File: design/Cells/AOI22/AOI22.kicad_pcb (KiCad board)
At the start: 2 copper layers, 8 parts, among them P1 Q_PJFET_GSD, P2 Q_PJFET_GSD, P3 Q_PJFET_GSD, P4 Q_PJFET_GSD

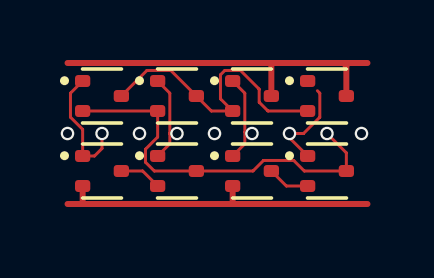
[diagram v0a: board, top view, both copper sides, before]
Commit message: Swap A and B pads in NAND footprint Polishing of AOI22 PCB, proper placement of the pins
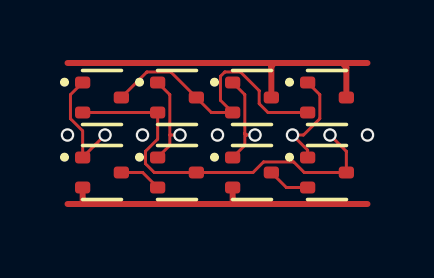
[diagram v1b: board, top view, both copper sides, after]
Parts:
- moved N1 0.05 mm to (1.15, 3.60)
- moved N2 0.05 mm to (3.65, 3.60)
- moved N3 0.05 mm to (6.15, 3.60)
- moved N4 0.05 mm to (8.65, 3.60)
- moved P1 0.05 mm to (1.15, 1.10)
- moved P2 0.05 mm to (3.65, 1.10)
- moved P3 0.05 mm to (6.15, 1.10)
- moved P4 0.05 mm to (8.65, 1.10)

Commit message: All gates layout on a strict 2.5mm grid. Flipped versions of all three layouts
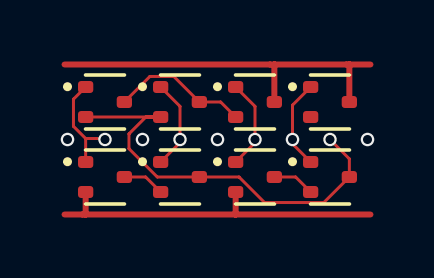
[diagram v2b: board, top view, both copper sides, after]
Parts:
- moved N1 0.18 mm to (1.25, 3.75)
- moved N2 0.18 mm to (3.75, 3.75)
- moved P1 0.18 mm to (1.25, 1.25)
- moved P2 0.18 mm to (3.75, 1.25)
- moved N3 0.18 mm to (6.25, 3.75)
- moved N4 0.18 mm to (8.75, 3.75)
- moved P3 0.18 mm to (6.25, 1.25)
- moved P4 0.18 mm to (8.75, 1.25)
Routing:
- net Net-(P1-D): track 9.78 -> 4.62 mm
- net Y: track 13.0 -> 14.2 mm
- net GND: track 11.1 -> 11.7 mm
- net D: track 3.54 -> 3.00 mm

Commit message: flip the cells to share power lines
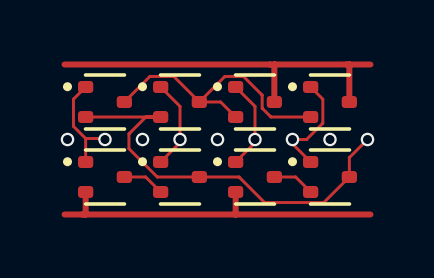
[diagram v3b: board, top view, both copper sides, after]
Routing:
- net Net-(P1-D): track 4.62 -> 9.50 mm
- net D: track 3.00 -> 3.61 mm
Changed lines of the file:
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@@
 	)
 	(via
-		(at 10 2.5)
+		(at 5 2.5)
 		(size 0.45)
 		(drill 0.3)
@@
 	)
 	(via
-		(at 5 2.5)
+		(at 0 2.5)
 		(size 0.45)
 		(drill 0.3)
@@
 	)
 	(via
-		(at 0 2.5)
+		(at 8.75 2.5)
 		(size 0.45)
 		(drill 0.3)
@@
 	)
 	(segment
+		(start 9.395 3.75)
+		(end 9.395 3.105)
+		(width 0.1)
+		(layer "F.Cu")
+		(net 5)
+	)
+	(segment
 		(start 6.568738 4.601)
 		(end 5.717738 3.75)
@@
 	)
 	(segment
-		(start 9.395 3.145)
-		(end 9.395 3.75)
-		(width 0.1)
-		(layer "F.Cu")
-		(net 5)
-	)
-	(segment
-		(start 8.75 2.5)
-		(end 9.395 3.145)
+		(start 9.395 3.105)
+		(end 10 2.5)
 		(width 0.1)
 		(layer "F.Cu")
@@
 	)
 	(via
-		(at 8.75 2.5)
+		(at 10 2.5)
 		(size 0.45)
 		(drill 0.3)
@@
 	)
 	(segment
+		(start 8.511 1.956738)
+		(end 7.967738 2.5)
+		(width 0.1)
+		(layer "F.Cu")
+		(net 8)
+	)
+	(segment
+		(start 8.105 0.75)
+		(end 8.511 1.156)
+		(width 0.1)
+		(layer "F.Cu")
+		(net 8)
+	)
+	(segment
 		(start 7.5 2.5)
 		(end 7.5 2.645)
@@
 	)
 	(segment
-		(start 8.105 0.75)
-		(end 7.5 1.355)
-		(width 0.1)
-		(layer "F.Cu")
-		(net 8)
-	)
-	(segment
-		(start 7.5 1.355)
+		(start 7.967738 2.5)
 		(end 7.5 2.5)
+		(width 0.1)
+		(layer "F.Cu")
+		(net 8)
+	)
+	(segment
+		(start 8.511 1.156)
+		(end 8.511 1.956738)
 		(width 0.1)
 		(layer "F.Cu")
@@
 	)
 	(segment
+		(start 6.782262 1.75)
+		(end 8.105 1.75)
+		(width 0.1)
+		(layer "F.Cu")
+		(net 9)
+	)
+	(segment
 		(start 2.746 0.399)
 		(end 3.544 0.399)
@@
 		(width 0.1)
 		(layer "F.Cu")
+		(net 9)
+	)
+	(segment
+		(start 6.489 1.021262)
+		(end 6.489 1.456738)
+		(width 0.1)
+		(layer "F.Cu")
+		(net 9)
+	)
+	(segment
+		(start 6.489 1.456738)
+		(end 6.782262 1.75)
+		(width 0.1)
+		(layer "F.Cu")
+		(net 9)
+	)
+	(segment
+		(start 4.395 1.25)
+		(end 5.246 0.399)
+		(width 0.1)
+		(layer "F.Cu")
+		(net 9)
+	)
+	(segment
+		(start 5.246 0.399)
+		(end 5.866738 0.399)
+		(width 0.1)
+		(layer "F.Cu")
+		(net 9)
+	)
+	(segment
+		(start 5.866738 0.399)
+		(end 6.489 1.021262)
+		(width 0.1)
+		(layer "F.Cu")
